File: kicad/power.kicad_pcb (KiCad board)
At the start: 2 copper layers, 84.1 x 61.7 mm, 48 parts, among them J1 Bus_PCI_Express_x1, J201 USB_C_Receptacle_USB2.0_16P, U402 MP2672GD-0000-Z, U403 Battery (MR-30), U501 TPS63070RNMR, U601 TPS63070RNMR

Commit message: start via stitching
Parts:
- added D501: LED, LED_SMD:LED_0603_1608Metric, F.Cu at (169.2, 118.4)
- added R505: 1k, Resistor_SMD:R_0402_1005Metric, F.Cu at (169.1, 114.4)
- moved D1 126.6 mm to (162.4, 118.4), turned to 90 degrees
- moved R11 125.4 mm to (162.4, 114.6), turned to -90 degrees
- moved R602 96.7 mm to (166.0, 80.3), turned to -90 degrees
- moved C603 89.5 mm to (162.4, 81.3)
- moved C607 86.1 mm to (159.9, 78.4)
- moved C608 85.3 mm to (160.1, 85.4)
- moved C602 84.9 mm to (154.2, 88.0), turned to 90 degrees
- moved L601 84.0 mm to (154.4, 81.6), turned to 90 degrees
- moved C605 83.4 mm to (157.5, 73.1)
- moved R601 82.4 mm to (160.1, 87.7)
- moved C604 81.1 mm to (156.7, 76.0), turned to 180 degrees
- moved C601 80.5 mm to (150.5, 88.1), turned to 90 degrees
- moved C606 79.7 mm to (151.8, 71.0), turned to 180 degrees
- moved R503 73.8 mm to (144.8, 81.5), turned to 90 degrees
- moved R501 69.4 mm to (137.7, 85.8), turned to 90 degrees
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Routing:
- net +3.3V: track 7.85 -> 87.5 mm, vias 2 -> 8
- net +5V: track 5.71 -> 83.2 mm, vias 3 -> 6
- net /VBUS: track 32.8 -> 57.5 mm
- net /power/VSYS: track 37.5 -> 54.0 mm
- net AGND: track 21.1 -> 36.2 mm
- net Net-(U601-EN): track 0.00 -> 15.1 mm
- net GND: track 9.00 -> 23.5 mm, vias 0 -> 352
- net Net-(U501-FB): track 0.00 -> 8.31 mm
- net Net-(U501-EN): track 0.00 -> 6.54 mm
- net Net-(U601-PG): track 0.00 -> 6.11 mm
- net Net-(U501-L2): track 0.00 -> 5.98 mm
- net Net-(U501-L1): track 0.00 -> 5.82 mm
- net Net-(U402-MID): track 13.2 -> 8.59 mm
- net Net-(U402-BATT): track 13.7 -> 9.10 mm
- net Net-(U501-PG): track 0.00 -> 4.54 mm
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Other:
- board text added: "3.3V"
- board text added: "5V"

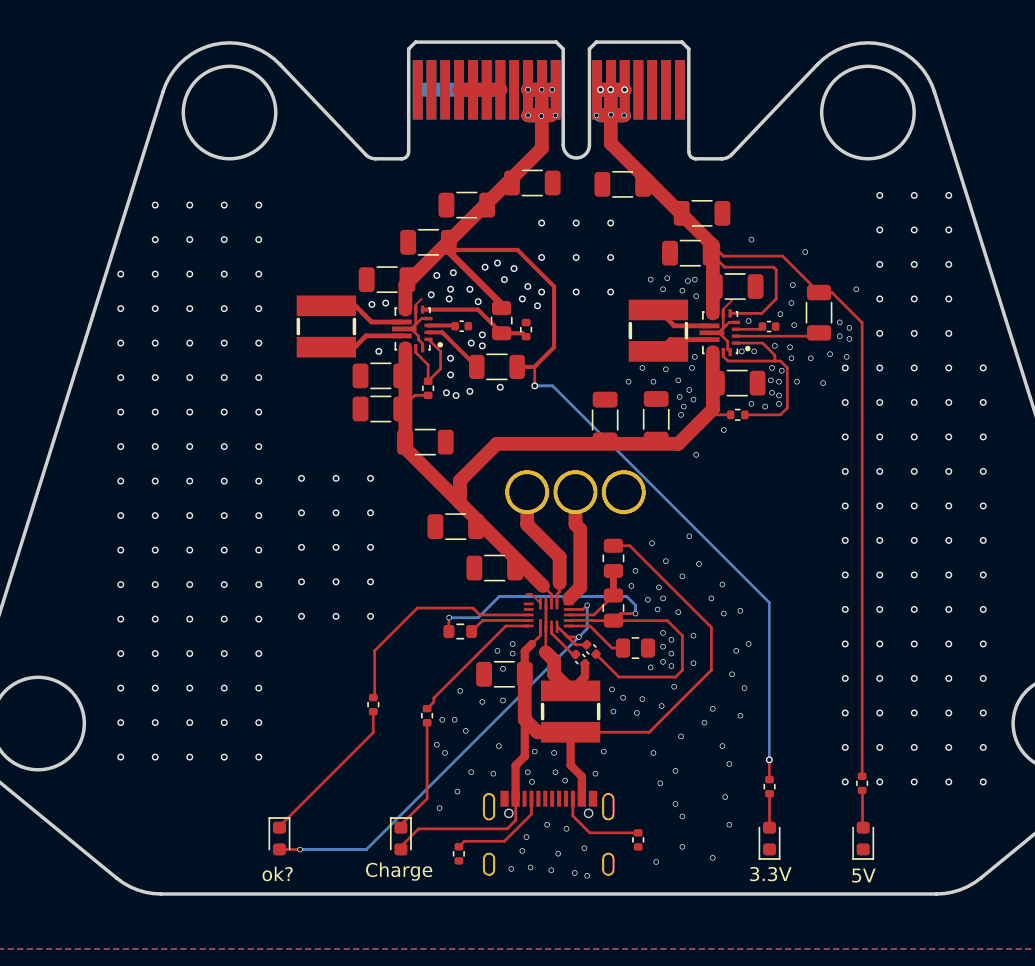
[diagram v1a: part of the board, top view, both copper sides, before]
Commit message: finish via stitching and routing
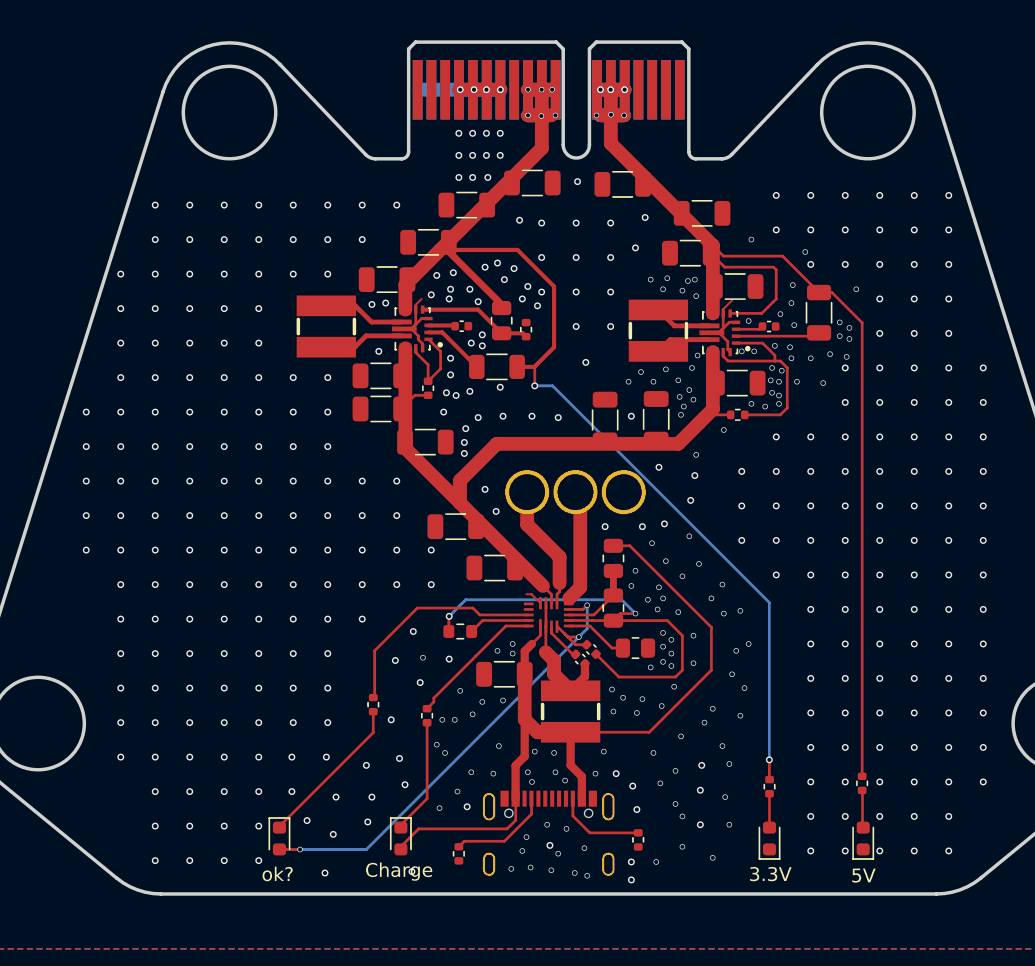
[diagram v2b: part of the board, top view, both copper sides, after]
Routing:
- net GND: vias 352 -> 500

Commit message: export final production files for 0.1.0
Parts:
- added C430: 22u, Capacitor_SMD:C_1206_3216Metric, F.Cu at (145.2, 97.6)
- added G***: LOGO, LOGO, F.Cu at (167.8, 96.0)
- added R460: 33m, Resistor_SMD:R_1206_3216Metric, F.Cu at (149.1, 98.1)
- added R461: 33m, Resistor_SMD:R_1206_3216Metric, F.Cu at (151.6, 98.1)
- R503: footprint Resistor_SMD:R_0402_1005Metric -> Resistor_SMD:R_0805_2012Metric
- moved R404 4.78 mm to (154.9, 101.0), turned to 180 degrees
- moved C409 3.30 mm to (139.3, 99.6)
- moved C408 1.89 mm to (138.4, 97.2)
- moved R11 1.19 mm to (163.6, 114.7)
- moved D1 1.19 mm to (163.6, 118.4)
- moved R503 0.66 mm to (145.0, 80.9)
- moved R405 0.58 mm to (151.4, 102.2)
- moved R409 0.41 mm to (152.6, 105.0)
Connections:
- U403 pad 2: Net-(U402-MID) -> Net-(R460-Pad2)
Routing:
- net Net-(R460-Pad2): track 0.00 -> 6.59 mm
- net /VBUS: track 57.5 -> 51.1 mm
- net GND: track 23.5 -> 28.6 mm, vias 500 -> 497
- net Net-(U402-MID): track 8.59 -> 5.24 mm
- net /power/VSYS: track 54.0 -> 56.6 mm
- net Net-(U402-VLIM): track 5.60 -> 6.87 mm
- net AGND: track 35.7 -> 36.7 mm
- net +3.3V: track 87.5 -> 88.1 mm
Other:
- board text added: "+-"
- board text added: "."
- board text added: "power 0.1.0"
